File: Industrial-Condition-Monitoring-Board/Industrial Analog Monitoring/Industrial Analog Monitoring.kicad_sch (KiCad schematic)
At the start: 60 parts, among them J1 +12V i/p, J2 Temperature Sensor Input, J3 LDR input, J4 Pressure input, Q1 BC547, Q2 BC547, Q3 BC547, Q4 BC547, U1 LM7805_TO220, U2 LM358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

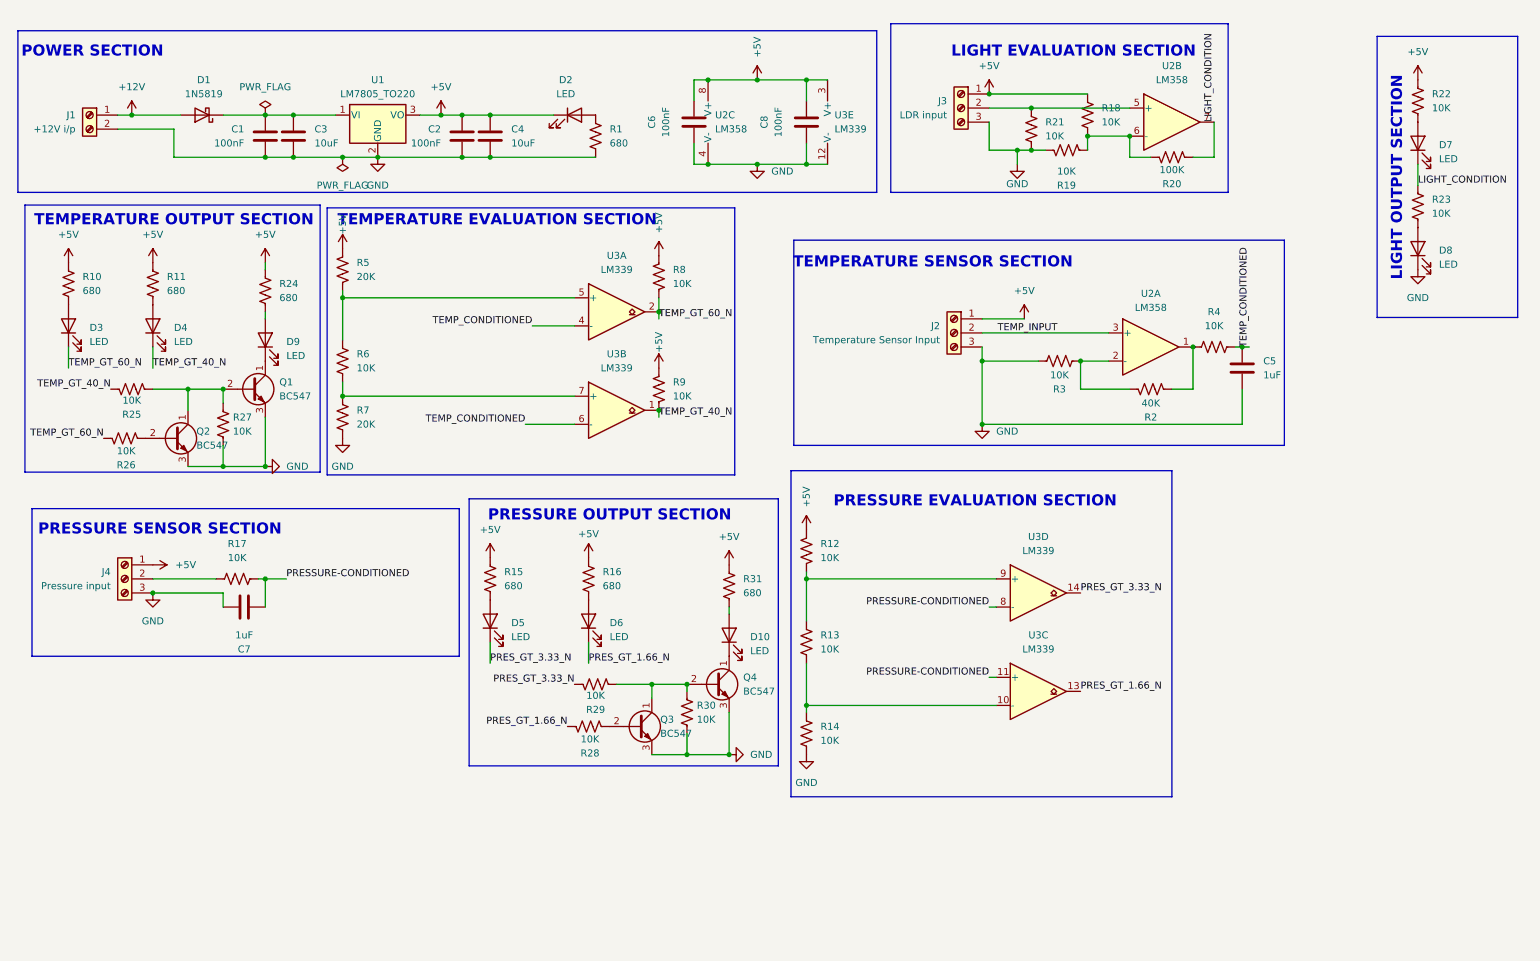
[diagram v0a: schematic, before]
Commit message: Added Industrial Condition Monitoring Board project
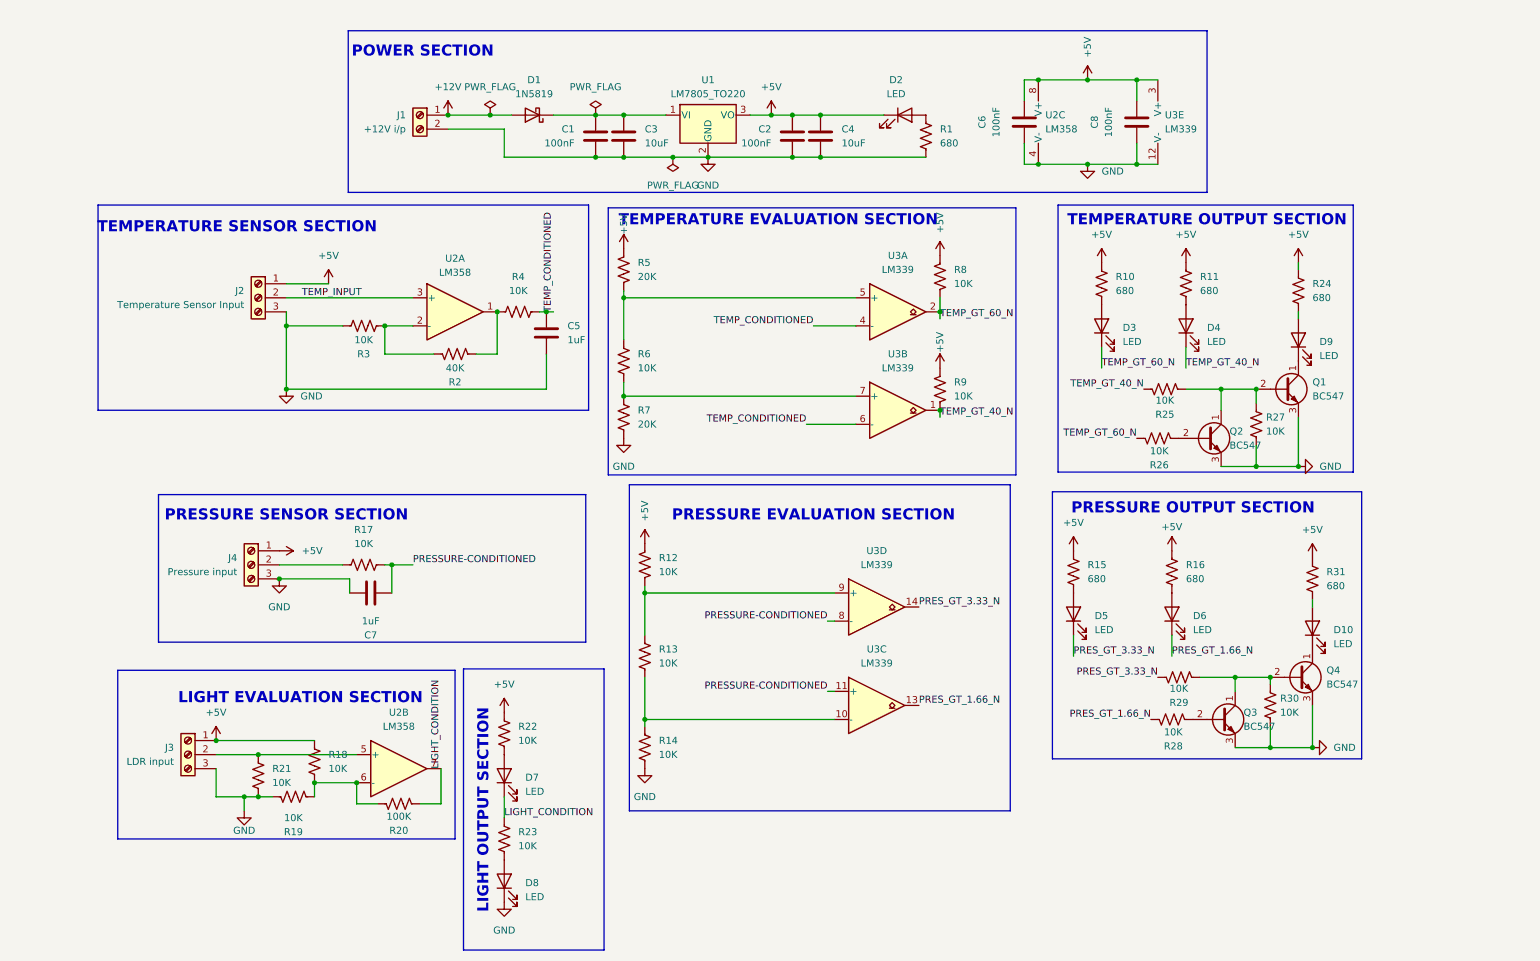
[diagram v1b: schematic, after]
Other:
- moved on the sheet: C1, C2, C3, C4, C5, C6, C7, C8, D1, D10, D2, D3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
